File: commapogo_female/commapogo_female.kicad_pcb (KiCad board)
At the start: 4 copper layers, 40.6 x 22.2 mm, 6 parts, among them J1 Conn_02x07_Row_Letter_Last, J2 Conn_02x12_Row_Letter_Last

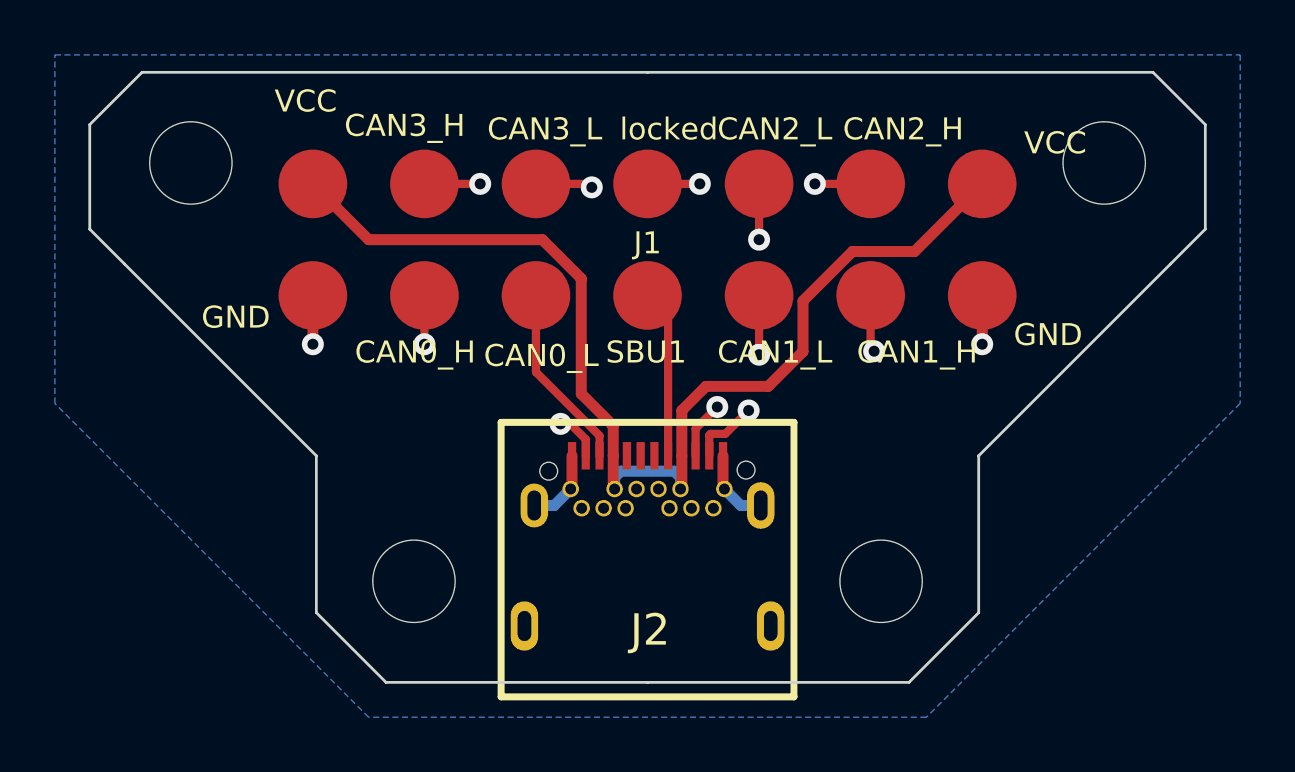
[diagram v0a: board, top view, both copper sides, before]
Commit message: redo pcb design add more ground planes
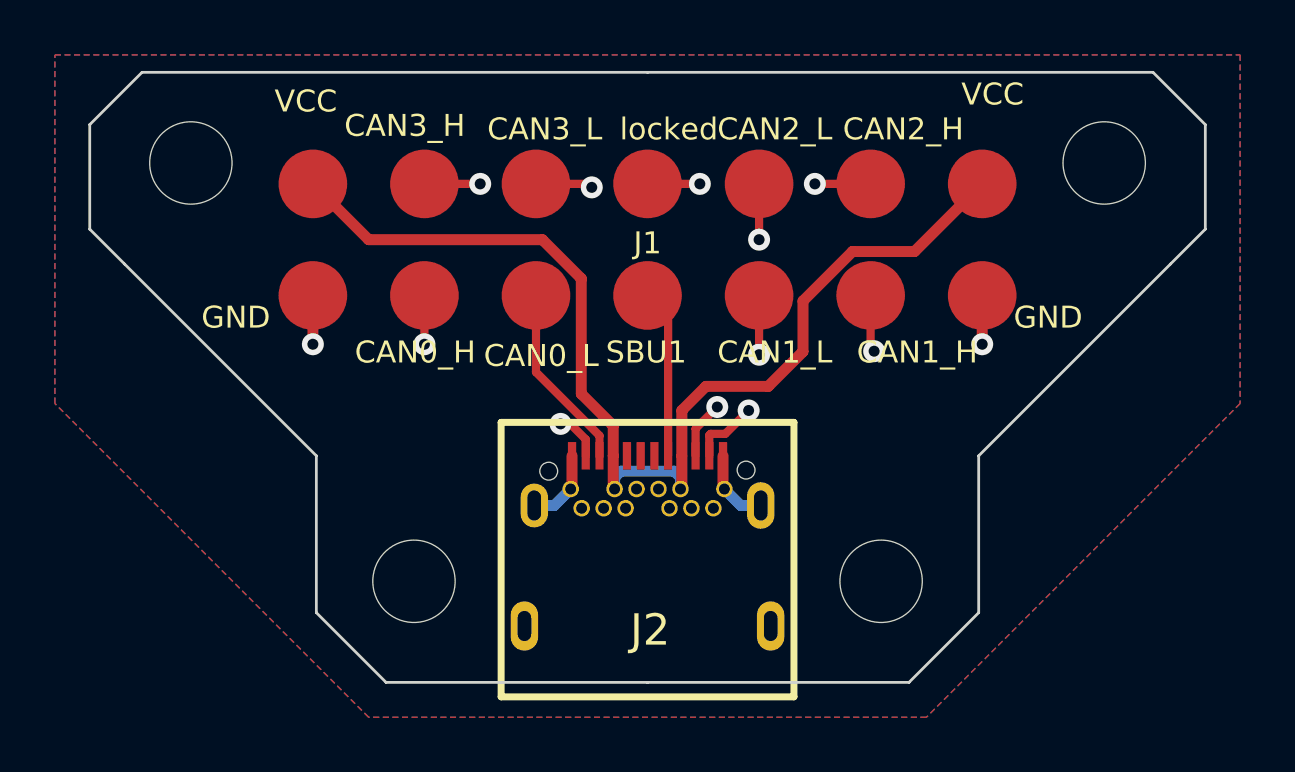
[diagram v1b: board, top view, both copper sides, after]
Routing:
- added copper zone on F.Cu, net GND
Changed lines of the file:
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@@
         (effects (font (size 1 1) (thickness 0.15)))
     )
-    (fp_text user "VCC" (at 13.716 -7.112 unlocked) (layer "F.SilkS")
+    (fp_text user "VCC" (at 11.43 -8.89 unlocked) (layer "F.SilkS")
         (effects (font (size 0.8 0.8) (thickness 0.1)) (justify left bottom))
     )
@@
     (effects (font (size 0.8 0.8) (thickness 0.1)) (justify left bottom))
   )
-  (gr_text "GND" (at 153.67 83.693) (layer "F.SilkS")
+  (gr_text "GND" (at 153.67 83.058) (layer "F.SilkS")
     (effects (font (size 0.8 0.8) (thickness 0.1)) (justify left bottom))
   )
@@
   (segment (start 138.557 85.471) (end 138.557 82.042) (width 0.3) (layer "In1.Cu") (net 17))
   (segment (start 137.935 89.54) (end 138.135 89.34) (width 0.3) (layer "In1.Cu") (net 17))
+  (zone (net 4) (net_name "GND") (layer "F.Cu") (hatch edge 0.5)
+    (priority 1)
+    (connect_pads (clearance 0.5))
+    (min_thickness 0.25) (filled_areas_thickness no)
+    (fill yes (thermal_gap 0.5) (thermal_bridge_width 0.5))
+    (polygon
+      (pts
+        (xy 118.745 73.025)
+        (xy 161.925 73.025)
+        (xy 161.925 85.725)
+        (xy 150.495 97.155)
+        (xy 130.175 97.155)
+        (xy 118.745 85.725)
+      )
+    )
+  )
   (zone locked (net 4) (net_name "GND") (layer "B.Cu") (hatch edge 0.5)
     (connect_pads (clearance 0.5))
